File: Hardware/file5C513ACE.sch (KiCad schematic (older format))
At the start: 69 parts, among them J1 GATE_2, J2 GATE_3, J3 GATE_1, Q1 MMBT3904, Q2 MMBT3904, Q3 MMBT3904, SW1 Frequency Adjust, SW10 PROG, SW11 PROG, SW2 PROG, SW3 PROG, SW4 PROG, SW5 PROG, SW6 PROG, SW7 RST, SW8 PROG, SW9 PROG, U1 TLC5947DAP

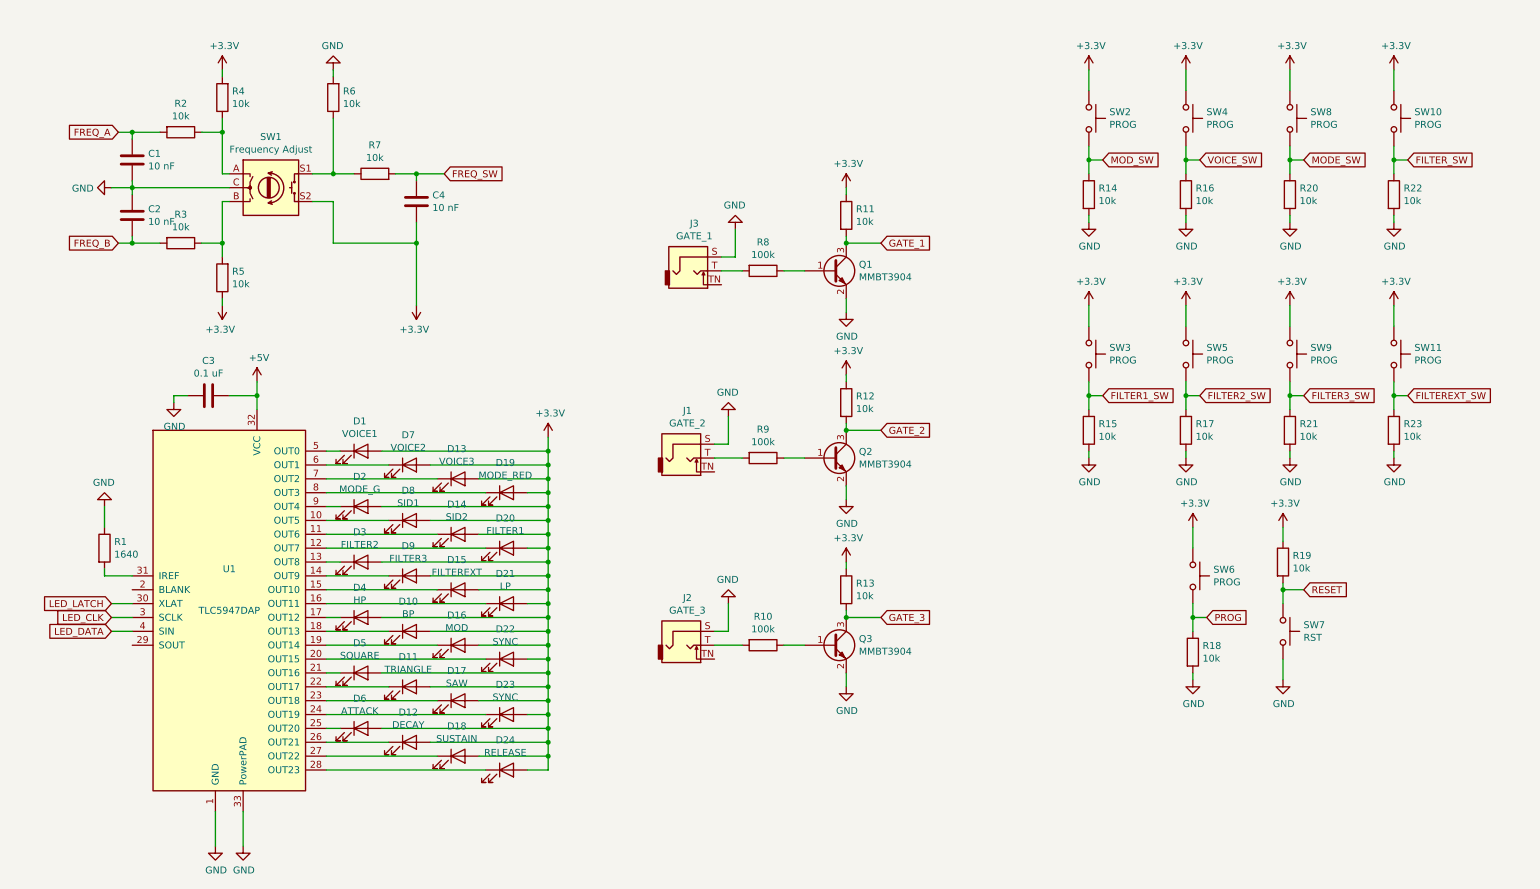
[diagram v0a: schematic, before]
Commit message: Started board layout
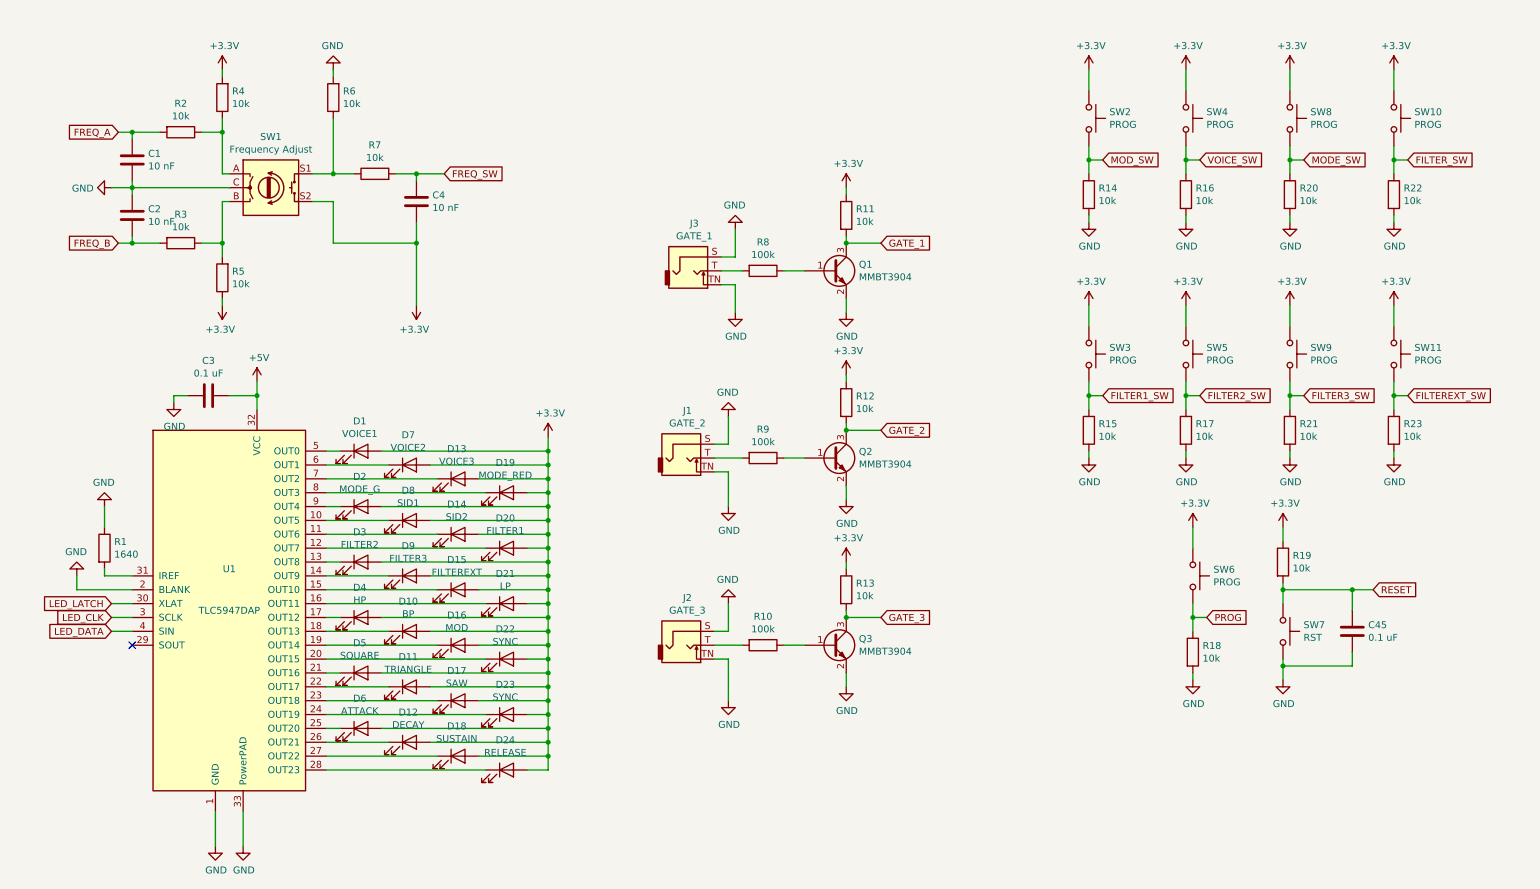
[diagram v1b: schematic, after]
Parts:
- added C45: 0.1 uF, Capacitors_SMD:C_0603, symbol Device:C
- C1, C2, C3, C4: footprint (none) -> Capacitors_SMD:C_0603
- U1: footprint Package_SO:HTSSOP-32-1EP_6.1x11mm_P0.65mm_EP5.2x11mm_Mask4.11x4.36mm_ThermalVias -> Housings_SSOP:HTSSOP-32_6.1x11mm_Pitch0.65mm_ThermalPad
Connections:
- net GND: now also J1.TN, J2.TN, J3.TN, U1.2 (BLANK), C45.2
- net RESET: now also C45.1
- no-connect marks 0 -> 1
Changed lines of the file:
@@
 F 0 "C1" H 1215 1496 50  0000 L CNN
 F 1 "10 nF" H 1215 1405 50  0000 L CNN
-F 2 "" H 1138 1300 50  0001 C CNN
+F 2 "Capacitors_SMD:C_0603" H 1138 1300 50  0001 C CNN
 F 3 "~" H 1100 1450 50  0001 C CNN
 	1    1100 1450
@@
 F 0 "C2" H 1215 1896 50  0000 L CNN
 F 1 "10 nF" H 1215 1805 50  0000 L CNN
-F 2 "" H 1138 1700 50  0001 C CNN
+F 2 "Capacitors_SMD:C_0603" H 1138 1700 50  0001 C CNN
 F 3 "~" H 1100 1850 50  0001 C CNN
 	1    1100 1850
@@
 F 0 "C4" H 3265 1796 50  0000 L CNN
 F 1 "10 nF" H 3265 1705 50  0000 L CNN
-F 2 "" H 3188 1600 50  0001 C CNN
+F 2 "Capacitors_SMD:C_0603" H 3188 1600 50  0001 C CNN
 F 3 "~" H 3150 1750 50  0001 C CNN
 	1    3150 1750
@@
 F 0 "U1" H 1800 5100 50  0000 C CNN
 F 1 "TLC5947DAP" H 1800 4800 50  0000 C CNN
-F 2 "Package_SO:HTSSOP-32-1EP_6.1x11mm_P0.65mm_EP5.2x11mm_Mask4.11x4.36mm_ThermalVias" H 1250 6350 50  0001 L CNN
+F 2 "Housings_SSOP:HTSSOP-32_6.1x11mm_Pitch0.65mm_ThermalPad" H 1250 6350 50  0001 L CNN
 F 3 "http://www.ti.com/lit/ds/symlink/tlc5947.pdf" H 1800 4750 50  0001 C CNN
 	1    1800 4750
@@
 F 0 "C3" V 1398 3150 50  0000 C CNN
 F 1 "0.1 uF" V 1489 3150 50  0000 C CNN
-F 2 "" H 1688 3000 50  0001 C CNN
+F 2 "Capacitors_SMD:C_0603" H 1688 3000 50  0001 C CNN
 F 3 "~" H 1650 3150 50  0001 C CNN
 	1    1650 3150
@@
 $EndComp
 Wire Wire Line
-	9400 5200 9400 5050
+	9400 5200 9400 5100
 $Comp
 L Device:R R?
@@
 Wire Wire Line
 	8750 4650 8750 4750
-Text GLabel 9550 4550 2    50   Input ~ 0
+Text GLabel 10050 4550 2    50   Input ~ 0
 RESET
 Wire Wire Line
-	9550 4550 9400 4550
+	10050 4550 9900 4550
 Wire Wire Line
 	9400 4500 9400 4550
@@
 Wire Wire Line
 	9450 3150 9450 3250
+$Comp
+L power:GND #PWR?
+U 1 1 5BED1C68
+P 5400 5350
+AR Path="/5BFD63E3/5BED1C68" Ref="#PWR?"  Part="1"
+AR Path="/5C5B0294/5BED1C68" Ref="#PWR?"  Part="1"
+AR Path="/5BFD63E3/5C513ACF/5BED1C68" Ref="#PWR02"  Part="1"
+F 0 "#PWR02" H 5400 5100 50  0001 C CNN
+F 1 "GND" H 5405 5177 50  0000 C CNN
+F 2 "" H 5400 5350 50  0001 C CNN
+F 3 "" H 5400 5350 50  0001 C CNN
+	1    5400 5350
+	1    0    0    -1
+$EndComp
+Wire Wire Line
+	5400 5350 5400 5050
+Wire Wire Line
+	5400 5050 5300 5050
+$Comp
+L power:GND #PWR?
+U 1 1 5BED990B
+P 5400 3950
+AR Path="/5BFD63E3/5BED990B" Ref="#PWR?"  Part="1"
+AR Path="/5C5B0294/5BED990B" Ref="#PWR?"  Part="1"
+AR Path="/5BFD63E3/5C513ACF/5BED990B" Ref="#PWR01"  Part="1"
+F 0 "#PWR01" H 5400 3700 50  0001 C CNN
+F 1 "GND" H 5405 3777 50  0000 C CNN
+F 2 "" H 5400 3950 50  0001 C CNN
+F 3 "" H 5400 3950 50  0001 C CNN
+	1    5400 3950
+	1    0    0    -1
+$EndComp
+Wire Wire Line
+	5400 3950 5400 3700
+Wire Wire Line
+	5400 3700 5300 3700
+$Comp
+L power:GND #PWR?
+U 1 1 5BEE18CE
+P 5450 2550
+AR Path="/5BFD63E3/5BEE18CE" Ref="#PWR?"  Part="1"
+AR Path="/5C5B0294/5BEE18CE" Ref="#PWR?"  Part="1"
+AR Path="/5BFD63E3/5C513ACF/5BEE18CE" Ref="#PWR03"  Part="1"
+F 0 "#PWR03" H 5450 2300 50  0001 C CNN
+F 1 "GND" H 5455 2377 50  0000 C CNN
+F 2 "" H 5450 2550 50  0001 C CNN
+F 3 "" H 5450 2550 50  0001 C CNN
+	1    5450 2550
+	1    0    0    -1
+$EndComp
+Wire Wire Line
+	5450 2550 5450 2350
+Wire Wire Line
+	5450 2350 5350 2350
+$Comp
+L Device:C C?
+U 1 1 5BF2EEEA
+P 9900 4850
+AR Path="/5BFD63E3/5BF2EEEA" Ref="C?"  Part="1"
+AR Path="/5BFD63E3/5C513ACF/5BF2EEEA" Ref="C45"  Part="1"
+F 0 "C45" H 10015 4896 50  0000 L CNN
+F 1 "0.1 uF" H 10015 4805 50  0000 L CNN
+F 2 "Capacitors_SMD:C_0603" H 9938 4700 50  0001 C CNN
+F 3 "~" H 9900 4850 50  0001 C CNN
+	1    9900 4850
+	1    0    0    -1
+$EndComp
+Wire Wire Line
+	9900 5000 9900 5100
+Wire Wire Line
+	9900 5100 9400 5100
+Connection ~ 9400 5100
+Wire Wire Line
+	9400 5100 9400 5050
+Wire Wire Line
+	9900 4700 9900 4550
+Connection ~ 9900 4550
+Wire Wire Line
+	9900 4550 9400 4550
+$Comp
+L power:GND #PWR?
+U 1 1 5BFDB517
+P 700 4450
+AR Path="/5BFD63E3/5BFDB517" Ref="#PWR?"  Part="1"
+AR Path="/5BFD63E3/5C513ACF/5BFDB517" Ref="#PWR0175"  Part="1"
+F 0 "#PWR0175" H 700 4200 50  0001 C CNN
+F 1 "GND" H 705 4277 50  0000 C CNN
+F 2 "" H 700 4450 50  0001 C CNN
+F 3 "" H 700 4450 50  0001 C CNN
+	1    700  4450
+	-1   0    0    1
+$EndComp
+Wire Wire Line
+	700  4450 700  4550
+Wire Wire Line
+	700  4550 1100 4550
+NoConn ~ 1100 4950
 $EndSCHEMATC

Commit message: Fixed issues with footprints
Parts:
- C1, C2, C3, C4, C45: footprint Capacitors_SMD:C_0603 -> Capacitor_SMD:C_0603_1608Metric
- U1: footprint Housings_SSOP:HTSSOP-32_6.1x11mm_Pitch0.65mm_ThermalPad -> Package_SO:HTSSOP-32-1EP_6.1x11mm_P0.65mm_EP5.2x11mm_Mask4.11x4.36mm_ThermalVias
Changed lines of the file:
@@
 F 0 "C1" H 1215 1496 50  0000 L CNN
 F 1 "10 nF" H 1215 1405 50  0000 L CNN
-F 2 "Capacitors_SMD:C_0603" H 1138 1300 50  0001 C CNN
+F 2 "Capacitor_SMD:C_0603_1608Metric" H 1138 1300 50  0001 C CNN
 F 3 "~" H 1100 1450 50  0001 C CNN
 	1    1100 1450
@@
 F 0 "C2" H 1215 1896 50  0000 L CNN
 F 1 "10 nF" H 1215 1805 50  0000 L CNN
-F 2 "Capacitors_SMD:C_0603" H 1138 1700 50  0001 C CNN
+F 2 "Capacitor_SMD:C_0603_1608Metric" H 1138 1700 50  0001 C CNN
 F 3 "~" H 1100 1850 50  0001 C CNN
 	1    1100 1850
@@
 F 0 "C4" H 3265 1796 50  0000 L CNN
 F 1 "10 nF" H 3265 1705 50  0000 L CNN
-F 2 "Capacitors_SMD:C_0603" H 3188 1600 50  0001 C CNN
+F 2 "Capacitor_SMD:C_0603_1608Metric" H 3188 1600 50  0001 C CNN
 F 3 "~" H 3150 1750 50  0001 C CNN
 	1    3150 1750
@@
 F 0 "U1" H 1800 5100 50  0000 C CNN
 F 1 "TLC5947DAP" H 1800 4800 50  0000 C CNN
-F 2 "Housings_SSOP:HTSSOP-32_6.1x11mm_Pitch0.65mm_ThermalPad" H 1250 6350 50  0001 L CNN
+F 2 "Package_SO:HTSSOP-32-1EP_6.1x11mm_P0.65mm_EP5.2x11mm_Mask4.11x4.36mm_ThermalVias" H 1250 6350 50  0001 L CNN
 F 3 "http://www.ti.com/lit/ds/symlink/tlc5947.pdf" H 1800 4750 50  0001 C CNN
 	1    1800 4750
@@
 F 0 "C3" V 1398 3150 50  0000 C CNN
 F 1 "0.1 uF" V 1489 3150 50  0000 C CNN
-F 2 "Capacitors_SMD:C_0603" H 1688 3000 50  0001 C CNN
+F 2 "Capacitor_SMD:C_0603_1608Metric" H 1688 3000 50  0001 C CNN
 F 3 "~" H 1650 3150 50  0001 C CNN
 	1    1650 3150
@@
 F 0 "C45" H 10015 4896 50  0000 L CNN
 F 1 "0.1 uF" H 10015 4805 50  0000 L CNN
-F 2 "Capacitors_SMD:C_0603" H 9938 4700 50  0001 C CNN
+F 2 "Capacitor_SMD:C_0603_1608Metric" H 9938 4700 50  0001 C CNN
 F 3 "~" H 9900 4850 50  0001 C CNN
 	1    9900 4850

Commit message: Added PJ398SM model
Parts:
- J1, J2, J3: footprint (none) -> Connector_Audio:Jack_3.5mm_QingPu_WQP-PJ398SM_Vertical_CircularHoles
- R1, R10, R11, R12, R13, R14, R15, R16, R17, R18, R19, R2, R20, R21, R22, R23, R3, R4, R5, R6, R7, R8, R9: footprint (none) -> Resistor_SMD:R_0603_1608Metric
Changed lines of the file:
@@
 F 0 "R2" V 1243 1250 50  0000 C CNN
 F 1 "10k" V 1334 1250 50  0000 C CNN
-F 2 "" V 1380 1250 50  0001 C CNN
+F 2 "Resistor_SMD:R_0603_1608Metric" V 1380 1250 50  0001 C CNN
 F 3 "~" H 1450 1250 50  0001 C CNN
 	1    1450 1250
@@
 F 0 "R4" H 1680 954 50  0000 R CNN
 F 1 "10k" H 1680 1045 50  0000 R CNN
-F 2 "" V 1680 1000 50  0001 C CNN
+F 2 "Resistor_SMD:R_0603_1608Metric" V 1680 1000 50  0001 C CNN
 F 3 "~" H 1750 1000 50  0001 C CNN
 	1    1750 1000
@@
 F 0 "R3" V 1243 2050 50  0000 C CNN
 F 1 "10k" V 1334 2050 50  0000 C CNN
-F 2 "" V 1380 2050 50  0001 C CNN
+F 2 "Resistor_SMD:R_0603_1608Metric" V 1380 2050 50  0001 C CNN
 F 3 "~" H 1450 2050 50  0001 C CNN
 	1    1450 2050
@@
 F 0 "R5" H 1680 2254 50  0000 R CNN
 F 1 "10k" H 1680 2345 50  0000 R CNN
-F 2 "" V 1680 2300 50  0001 C CNN
+F 2 "Resistor_SMD:R_0603_1608Metric" V 1680 2300 50  0001 C CNN
 F 3 "~" H 1750 2300 50  0001 C CNN
 	1    1750 2300
@@
 F 0 "R6" H 2480 954 50  0000 R CNN
 F 1 "10k" H 2480 1045 50  0000 R CNN
-F 2 "" V 2480 1000 50  0001 C CNN
+F 2 "Resistor_SMD:R_0603_1608Metric" V 2480 1000 50  0001 C CNN
 F 3 "~" H 2550 1000 50  0001 C CNN
 	1    2550 1000
@@
 F 0 "R7" V 3057 1550 50  0000 C CNN
 F 1 "10k" V 2966 1550 50  0000 C CNN
-F 2 "" V 2780 1550 50  0001 C CNN
+F 2 "Resistor_SMD:R_0603_1608Metric" V 2780 1550 50  0001 C CNN
 F 3 "~" H 2850 1550 50  0001 C CNN
 	1    2850 1550
@@
 F 0 "R1" H 970 4296 50  0000 L CNN
 F 1 "1640" H 970 4205 50  0000 L CNN
-F 2 "" V 830 4250 50  0001 C CNN
+F 2 "Resistor_SMD:R_0603_1608Metric" V 830 4250 50  0001 C CNN
 F 3 "~" H 900 4250 50  0001 C CNN
 	1    900  4250
@@
 F 0 "J3" H 5154 2592 50  0000 C CNN
 F 1 "GATE_1" H 5154 2501 50  0000 C CNN
-F 2 "" H 5150 2250 50  0001 C CNN
+F 2 "Connector_Audio:Jack_3.5mm_QingPu_WQP-PJ398SM_Vertical_CircularHoles" H 5150 2250 50  0001 C CNN
 F 3 "~" H 5150 2250 50  0001 C CNN
 	1    5150 2250
@@
 F 0 "J1" H 5104 3942 50  0000 C CNN
 F 1 "GATE_2" H 5104 3851 50  0000 C CNN
-F 2 "" H 5100 3600 50  0001 C CNN
+F 2 "Connector_Audio:Jack_3.5mm_QingPu_WQP-PJ398SM_Vertical_CircularHoles" H 5100 3600 50  0001 C CNN
 F 3 "~" H 5100 3600 50  0001 C CNN
 	1    5100 3600
@@
 F 0 "J2" H 5104 5292 50  0000 C CNN
 F 1 "GATE_3" H 5104 5201 50  0000 C CNN
-F 2 "" H 5100 4950 50  0001 C CNN
+F 2 "Connector_Audio:Jack_3.5mm_QingPu_WQP-PJ398SM_Vertical_CircularHoles" H 5100 4950 50  0001 C CNN
 F 3 "~" H 5100 4950 50  0001 C CNN
 	1    5100 4950
@@
 F 0 "R8" V 5443 2250 50  0000 C CNN
 F 1 "100k" V 5534 2250 50  0000 C CNN
-F 2 "" V 5580 2250 50  0001 C CNN
+F 2 "Resistor_SMD:R_0603_1608Metric" V 5580 2250 50  0001 C CNN
 F 3 "~" H 5650 2250 50  0001 C CNN
 	1    5650 2250
@@
 F 0 "R11" H 6320 1896 50  0000 L CNN
 F 1 "10k" H 6320 1805 50  0000 L CNN
-F 2 "" V 6180 1850 50  0001 C CNN
+F 2 "Resistor_SMD:R_0603_1608Metric" V 6180 1850 50  0001 C CNN
 F 3 "~" H 6250 1850 50  0001 C CNN
 	1    6250 1850
@@
 F 0 "R9" V 5443 3600 50  0000 C CNN
 F 1 "100k" V 5534 3600 50  0000 C CNN
-F 2 "" V 5580 3600 50  0001 C CNN
+F 2 "Resistor_SMD:R_0603_1608Metric" V 5580 3600 50  0001 C CNN
 F 3 "~" H 5650 3600 50  0001 C CNN
 	1    5650 3600
@@
 F 0 "R12" H 6320 3246 50  0000 L CNN
 F 1 "10k" H 6320 3155 50  0000 L CNN
-F 2 "" V 6180 3200 50  0001 C CNN
+F 2 "Resistor_SMD:R_0603_1608Metric" V 6180 3200 50  0001 C CNN
 F 3 "~" H 6250 3200 50  0001 C CNN
 	1    6250 3200
@@
 F 0 "R10" V 5443 4950 50  0000 C CNN
 F 1 "100k" V 5534 4950 50  0000 C CNN
-F 2 "" V 5580 4950 50  0001 C CNN
+F 2 "Resistor_SMD:R_0603_1608Metric" V 5580 4950 50  0001 C CNN
 F 3 "~" H 5650 4950 50  0001 C CNN
 	1    5650 4950
@@
 F 0 "R13" H 6320 4596 50  0000 L CNN
 F 1 "10k" H 6320 4505 50  0000 L CNN
-F 2 "" V 6180 4550 50  0001 C CNN
+F 2 "Resistor_SMD:R_0603_1608Metric" V 6180 4550 50  0001 C CNN
 F 3 "~" H 6250 4550 50  0001 C CNN
 	1    6250 4550
@@
 F 0 "R18" H 8820 5046 50  0000 L CNN
 F 1 "10k" H 8820 4955 50  0000 L CNN
-F 2 "" V 8680 5000 50  0001 C CNN
+F 2 "Resistor_SMD:R_0603_1608Metric" V 8680 5000 50  0001 C CNN
 F 3 "~" H 8750 5000 50  0001 C CNN
 	1    8750 5000
@@
 F 0 "R19" H 9470 4396 50  0000 L CNN
 F 1 "10k" H 9470 4305 50  0000 L CNN
-F 2 "" V 9330 4350 50  0001 C CNN
+F 2 "Resistor_SMD:R_0603_1608Metric" V 9330 4350 50  0001 C CNN
 F 3 "~" H 9400 4350 50  0001 C CNN
 	1    9400 4350
@@
 F 0 "R14" H 8070 1746 50  0000 L CNN
 F 1 "10k" H 8070 1655 50  0000 L CNN
-F 2 "" V 7930 1700 50  0001 C CNN
+F 2 "Resistor_SMD:R_0603_1608Metric" V 7930 1700 50  0001 C CNN
 F 3 "~" H 8000 1700 50  0001 C CNN
 	1    8000 1700
@@
 F 0 "R16" H 8770 1746 50  0000 L CNN
 F 1 "10k" H 8770 1655 50  0000 L CNN
-F 2 "" V 8630 1700 50  0001 C CNN
+F 2 "Resistor_SMD:R_0603_1608Metric" V 8630 1700 50  0001 C CNN
 F 3 "~" H 8700 1700 50  0001 C CNN
 	1    8700 1700
@@
 F 0 "R20" H 9520 1746 50  0000 L CNN
 F 1 "10k" H 9520 1655 50  0000 L CNN
-F 2 "" V 9380 1700 50  0001 C CNN
+F 2 "Resistor_SMD:R_0603_1608Metric" V 9380 1700 50  0001 C CNN
 F 3 "~" H 9450 1700 50  0001 C CNN
 	1    9450 1700
@@
 F 0 "R22" H 10270 1746 50  0000 L CNN
 F 1 "10k" H 10270 1655 50  0000 L CNN
-F 2 "" V 10130 1700 50  0001 C CNN
+F 2 "Resistor_SMD:R_0603_1608Metric" V 10130 1700 50  0001 C CNN
 F 3 "~" H 10200 1700 50  0001 C CNN
 	1    10200 1700
@@
 F 0 "R15" H 8070 3446 50  0000 L CNN
 F 1 "10k" H 8070 3355 50  0000 L CNN
-F 2 "" V 7930 3400 50  0001 C CNN
+F 2 "Resistor_SMD:R_0603_1608Metric" V 7930 3400 50  0001 C CNN
 F 3 "~" H 8000 3400 50  0001 C CNN
 	1    8000 3400
@@
 F 0 "R17" H 8770 3446 50  0000 L CNN
 F 1 "10k" H 8770 3355 50  0000 L CNN
-F 2 "" V 8630 3400 50  0001 C CNN
+F 2 "Resistor_SMD:R_0603_1608Metric" V 8630 3400 50  0001 C CNN
 F 3 "~" H 8700 3400 50  0001 C CNN
 	1    8700 3400
@@
 F 0 "R21" H 9520 3446 50  0000 L CNN
 F 1 "10k" H 9520 3355 50  0000 L CNN
-F 2 "" V 9380 3400 50  0001 C CNN
+F 2 "Resistor_SMD:R_0603_1608Metric" V 9380 3400 50  0001 C CNN
 F 3 "~" H 9450 3400 50  0001 C CNN
 	1    9450 3400
@@
 F 0 "R23" H 10270 3446 50  0000 L CNN
 F 1 "10k" H 10270 3355 50  0000 L CNN
-F 2 "" V 10130 3400 50  0001 C CNN
+F 2 "Resistor_SMD:R_0603_1608Metric" V 10130 3400 50  0001 C CNN
 F 3 "~" H 10200 3400 50  0001 C CNN
 	1    10200 3400
